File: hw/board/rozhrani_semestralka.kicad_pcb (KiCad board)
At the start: 2 copper layers, 152 x 46.9 mm, 62 parts, among them P1 DISPLAY_CONN, P2 DISPLAY_VCC_CON, P3 USB_B, U1 MCP2210, U2 MIC5504-3.3, U3 Joystick, U4 LM239, U5 CD4532, U6 NPIC6c596, U7 NE555, U8 BS800N, U9 BS800N

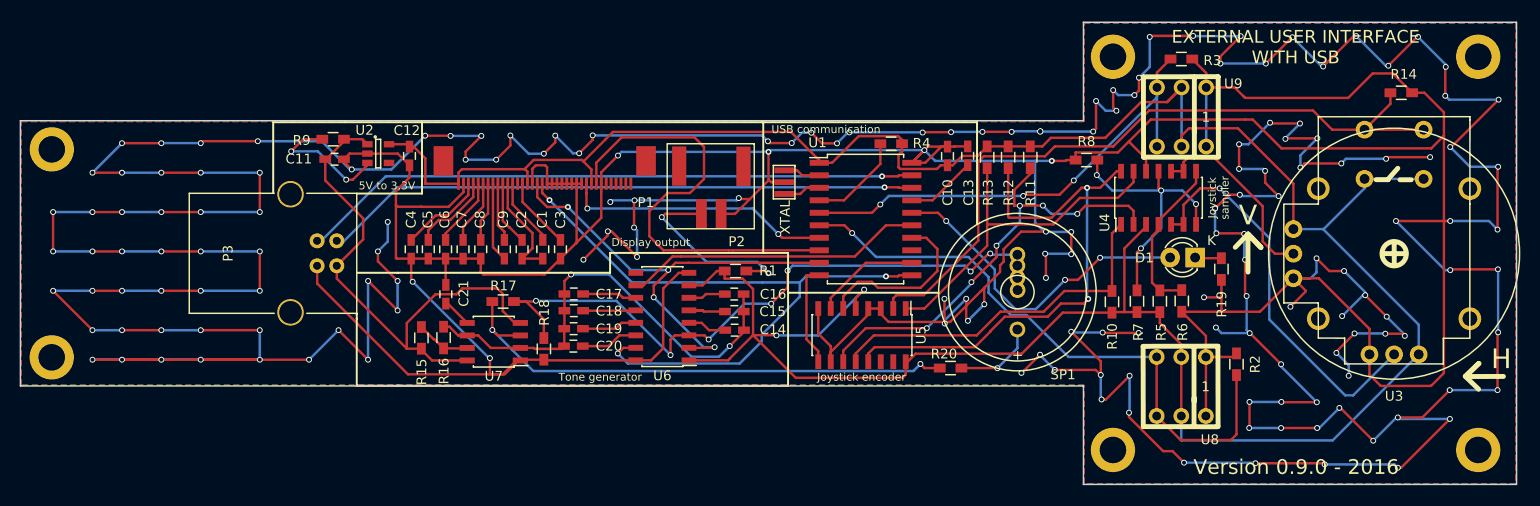
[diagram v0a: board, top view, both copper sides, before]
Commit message: Added hw board version 1.0.0 - buttons to another side and small updates
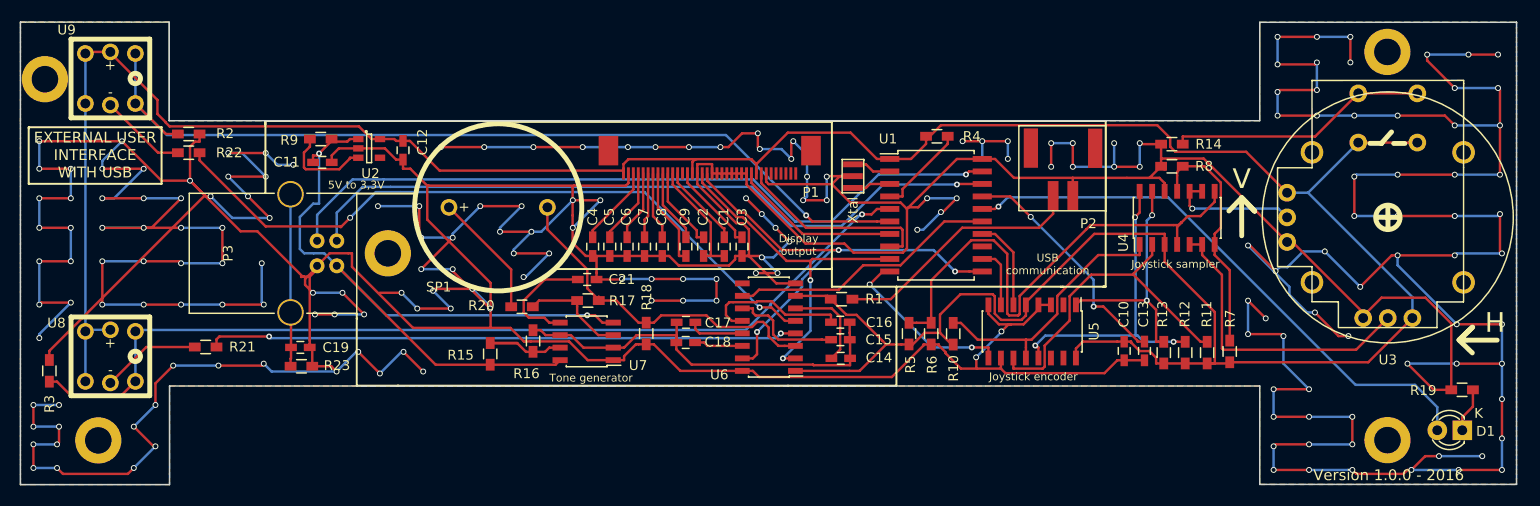
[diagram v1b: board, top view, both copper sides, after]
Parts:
- removed C20: 0, Capacitors_SMD:C_0603_HandSoldering
- removed the REF** at (77.9, 95.6)
- removed the REF** at (77.9, 116.8)
- removed the REF** at (222.8, 126.2)
- removed the REF** at (222.8, 86.2)
- removed the REF** at (185.7, 86.2)
- removed the REF** at (185.7, 126.2)
- removed XTAL: 12MHz, pcb:resonator12MHz
- added R21: 68, Resistors_SMD:R_0603_HandSoldering, F.Cu at (93.5, 115.7)
- added R22: 68, Resistors_SMD:R_0603_HandSoldering, F.Cu at (91.8, 96.0)
- added R23: 1M, Resistors_SMD:R_0603_HandSoldering, F.Cu at (103.2, 117.7)
- added REF**: MountingHole_2.7mm_M2.5_DIN965_Pad, Mounting_Holes:MountingHole_2.7mm_M2.5_DIN965_Pad, F.Cu at (213.6, 85.7)
- added REF**: MountingHole_2.7mm_M2.5_DIN965_Pad, Mounting_Holes:MountingHole_2.7mm_M2.5_DIN965_Pad, F.Cu at (213.6, 125.2)
- added REF**: MountingHole_2.7mm_M2.5_DIN965_Pad, Mounting_Holes:MountingHole_2.7mm_M2.5_DIN965_Pad, F.Cu at (82.6, 125.2)
- added REF**: MountingHole_2.7mm_M2.5_DIN965_Pad, Mounting_Holes:MountingHole_2.7mm_M2.5_DIN965_Pad, F.Cu at (77.2, 88.5)
- added REF**: MountingHole_2.7mm_M2.5_DIN965_Pad, Mounting_Holes:MountingHole_2.7mm_M2.5_DIN965_Pad, F.Cu at (112.0, 106.2)
- added Xtal: 12MHz, pcb:resonator12MHz, F.Cu at (159.3, 98.3)
- C19: value 0 -> 4,7nF
- D1: value LED -> L-1334SRT
- R1: value 390 -> 24
- R5: value 30K -> 22K
- R6: value 40K -> 33K
- R7: value 10K -> 33K
- R8: value 40K -> 3K
- SP1: footprint pcb:buzer -> pcb:Buzzer
- U6: value NPIC6c596 -> NPIC6C596
- U8, U9: value BS800N -> PB6149L; footprint pcb:BS-800-N -> pcb:PB6149L
- moved R3 119.3 mm to (77.6, 118.1), turned to 90 degrees
- moved R2 109.0 mm to (91.8, 94.1), turned to 180 degrees
- moved U9 108.9 mm to (83.8, 88.4), turned to 0 degrees
- moved U8 108.8 mm to (83.8, 116.7), turned to 0 degrees
- moved SP1 54.2 mm to (123.2, 101.5)
- moved R20 44.0 mm to (125.6, 111.6), turned to 180 degrees
- moved P2 35.8 mm to (180.6, 100.3)
- moved D1 32.3 mm to (221.2, 124.2)
- moved C19 27.8 mm to (103.1, 115.8)
- moved R19 27.4 mm to (221.2, 120.1), turned to 0 degrees
- moved R12 26.8 mm to (193.0, 116.3), turned to 270 degrees
- moved R11 26.8 mm to (195.2, 116.3), turned to 270 degrees
- moved R13 26.8 mm to (190.8, 116.3), turned to 270 degrees
- moved C13 26.8 mm to (188.9, 116.1), turned to 270 degrees
- moved C10 26.7 mm to (186.8, 116.1), turned to 270 degrees
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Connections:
- C10 pad 2: GND_HELP -> GND
- C11 pad 2: GND_HELP -> GND
- C12 pad 2: GND_HELP -> GND
- C13 pad 2: GND_HELP -> GND
- C14 pad 2: /REG1 -> /REG3
- C15 pad 2: /REG2 -> /REG4
- C16 pad 2: /REG3 -> /REG5
- C17 pad 2: /REG4 -> /REG6
- C18 pad 2: /REG5 -> /REG7
- C19 pad 1: Net-(C14-Pad1) -> Net-(C19-Pad1)
- C19 pad 2: /REG6 -> GND
- C21 pad 2: GND_HELP -> GND
- C3 pad 2: GND_HELP -> GND
- C4 pad 2: GND_HELP -> GND
- C5 pad 2: GND_HELP -> GND
- C6 pad 2: GND_HELP -> GND
- C7 pad 2: GND_HELP -> GND
- C8 pad 2: GND_HELP -> GND
- P1 pad 16: GND_HELP -> GND
- P1 pad 19: GND_HELP -> GND
- P1 pad 2: GND_HELP -> GND
- P1 pad 20: GND_HELP -> GND
- P1 pad 21: GND_HELP -> GND
- P1 pad 22: GND_HELP -> GND
- P1 pad 23: GND_HELP -> GND
- P1 pad 24: GND_HELP -> GND
- P1 pad 25: GND_HELP -> GND
- P1 pad 26: GND_HELP -> GND
- P1 pad 30: GND_HELP -> GND
- P2 pad 2: GND_HELP -> GND
- P3 pad 4: GND_HELP -> GND
- P3 pad 5: Net-(P3-Pad5) -> Net-(C19-Pad1)
- R14 pad 1: GND_HELP -> GND
- R14 pad 2: /JOY_C -> Net-(R14-Pad2)
- R18 pad 1: GND_HELP -> GND
- R19 pad 1: GND_HELP -> GND
- R2 pad 1: GND_HELP -> GND
- R3 pad 1: GND_HELP -> /BUT1
- R3 pad 2: /BUT1 -> GND
- R6 pad 1: GND_HELP -> GND
- R8 pad 1: GND_HELP -> GND
- U1 pad 20: GND_HELP -> GND
- U2 pad 2: GND_HELP -> GND
- U3 pad 1: /JOY_C -> Net-(R14-Pad2)
- U3 pad 2: /JOY_C -> Net-(R14-Pad2)
- U3 pad 7: GND_HELP -> GND
- U3 pad 8: GND_HELP -> GND
- U4 pad 12: GND_HELP -> GND
- U5 pad 10: GND_HELP -> GND
- U5 pad 3: GND_HELP -> GND
- U5 pad 4: GND_HELP -> GND
- U5 pad 8: GND_HELP -> GND
- U6 pad 16: GND_HELP -> GND
- U6 pad 8: GND_HELP -> GND
- U7 pad 1: GND_HELP -> GND
- U8 pad 1: GND_HELP -> +3V3
- U8 pad 2: +3V3 -> /BUT1
- U8 pad 3: /BUT2 -> +3V3
- U9 pad 1: GND_HELP -> +3V3
- U9 pad 2: +3V3 -> /BUT2
- U9 pad 3: /BUT1 -> +3V3
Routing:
- net GND: track 0.00 -> 1130.6 mm, vias 0 -> 195
- net GND_HELP: track 1128.7 -> 0.00 mm, vias 176 -> 0
- net /JOY_C: track 73.2 -> 0.00 mm
- net /REG2: track 5.54 -> 71.1 mm, vias 0 -> 2
- net /REG1: track 4.20 -> 60.0 mm, vias 0 -> 2
- net /BUT1: track 49.6 -> 96.8 mm, vias 3 -> 1
- net Net-(R17-Pad2): track 53.6 -> 10.7 mm, vias 2 -> 0
- net /Left: track 16.6 -> 53.1 mm
- net /REG0: track 70.0 -> 35.8 mm, vias 7 -> 0
- net /BUT2: track 62.2 -> 92.3 mm
- net +3V3: track 296.3 -> 324.2 mm, vias 2 -> 0
- net Net-(R14-Pad2): track 0.00 -> 26.4 mm
- net //CE: track 45.1 -> 20.3 mm
- net VCC: track 54.6 -> 79.1 mm, vias 0 -> 2
- net /SIGNAL_LED: track 33.6 -> 57.9 mm, vias 3 -> 1
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- added copper zone on B.Cu, net GND
- added copper zone on F.Cu, net GND
- removed copper zone on B.Cu, net GND_HELP
- removed copper zone on F.Cu, net GND_HELP
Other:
- board size 152 x 46.9 mm -> 152 x 47 mm
- board text added: "Version 1.0.0 - 2016"
- board text removed: "Version 0.9.0 - 2016"
